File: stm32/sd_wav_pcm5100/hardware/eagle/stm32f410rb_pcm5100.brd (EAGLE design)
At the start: 46 x 58.2 mm, 33 parts, among them IC1 STM32F410_8_B_LQFP64, U5 PCM5100

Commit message: added dirtypcb gerbers
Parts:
- C28, C29: value 2200pF -> 2.2nF
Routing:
- net N$11: track 0.00 -> 208.3 mm
- net VCC: track 257.2 -> 261.4 mm
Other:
- board size 46 x 58.2 mm -> 46.1 x 58.2 mm

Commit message: refactored pcb
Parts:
- JP2: value M023.5MM -> Vsupply - 3.3Vcc
- MMC1: value MICROSD_AMPHENOL -> Amphenol
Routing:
- net N$11: track 208.3 -> 0.00 mm
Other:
- board text added: "+3V3"
- board text added: "3V3"
- board text added: "GND"
- board text added: "NRST"
- board text added: "OUTL"
- board text added: "OUTR"
- board text added: "STANDBY"
- board text added: "SWO"
- board text added: "TCK"
- board text added: "TMS"
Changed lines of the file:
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@@
 <wire x1="46.1772" y1="0" x2="0.127" y2="0" width="0.4064" layer="20"/>
 <wire x1="0.127" y1="0" x2="0.127" y2="58.1152" width="0.4064" layer="20"/>
+<text x="1.8288" y="15.0622" size="0.6096" layer="21" ratio="14" rot="MR270">TMS</text>
+<text x="1.8288" y="17.8562" size="0.6096" layer="21" ratio="14" rot="MR270">GND</text>
+<text x="1.778" y="20.193" size="0.6096" layer="21" ratio="14" rot="MR270">3V3</text>
+<text x="1.7272" y="22.5552" size="0.6096" layer="21" ratio="14" rot="MR270">TCK</text>
+<text x="1.651" y="25.3238" size="0.6096" layer="21" ratio="14" rot="MR270">SWO</text>
+<text x="1.651" y="28.2702" size="0.6096" layer="21" ratio="14" rot="MR270">NRST</text>
+<text x="44.196" y="4.4958" size="0.6096" layer="21" ratio="14" rot="MR270">GND</text>
+<text x="44.0944" y="8.7122" size="0.6096" layer="21" ratio="14" rot="MR270">+3V3</text>
+<text x="30.8356" y="57.2008" size="0.6096" layer="21" ratio="14" rot="MR180">GND</text>
+<text x="34.1884" y="57.2516" size="0.6096" layer="21" ratio="14" rot="MR180">OUTR</text>
+<text x="27.3812" y="57.2516" size="0.6096" layer="21" ratio="14" rot="MR180">OUTL</text>
+<text x="22.5552" y="57.2262" size="0.6096" layer="21" ratio="14" rot="MR180">STANDBY</text>
 </plain>
 <attributes>
@@
 </element>
 <element name="JP1" library="pinhead" package="1X06" value="SWD" x="4.1275" y="20.6375" smashed="yes" rot="R270">
-<attribute name="NAME" x="1.3843" y="20.2311" size="0.6096" layer="25" ratio="10" rot="R270"/>
-<attribute name="VALUE" x="1.3081" y="24.2443" size="0.6096" layer="27" rot="R270"/>
+<attribute name="NAME" x="3.2385" y="12.4587" size="0.6096" layer="26" ratio="10" rot="MR270"/>
+<attribute name="VALUE" x="4.7371" y="12.5349" size="0.6096" layer="28" rot="MR270"/>
 </element>
 <element name="R2" library="SparkFun-Passives" package="0805" value="10K" x="7.239" y="37.2745" smashed="yes" rot="MR180">
@@
 <attribute name="VALUE" x="21.082" y="42.1005" size="0.6096" layer="28" rot="MR0"/>
 </element>
-<element name="MMC1" library="microsd_amphenol" package="MICROSD_AMPHENOL" value="MICROSD_AMPHENOL" x="34.163" y="18.0975" smashed="yes" rot="MR270"/>
+<element name="MMC1" library="microsd_amphenol" package="MICROSD_AMPHENOL" value="Amphenol" x="34.163" y="18.0975" smashed="yes" rot="MR270"/>
 <element name="R3" library="SparkFun-Passives" package="0805" value="22" x="6.8326" y="15.1384" smashed="yes" rot="MR0">
 <attribute name="NAME" x="9.6012" y="15.4305" size="0.6096" layer="26" rot="MR0"/>
@@
 </element>
 <element name="JP7" library="SparkFun-Connectors" package="SCREWTERMINAL-3.5MM-4" value="BTN_8-11" x="4.826" y="6.35" smashed="yes">
-<attribute name="NAME" x="3.556" y="8.89" size="0.6096" layer="25"/>
-<attribute name="VALUE" x="3.556" y="7.62" size="0.6096" layer="27"/>
+<attribute name="NAME" x="9.8806" y="10.9982" size="0.6096" layer="26" rot="MR180"/>
+<attribute name="VALUE" x="11.6332" y="1.4732" size="0.6096" layer="28" rot="MR0"/>
 </element>
 <element name="JP3" library="SparkFun-Connectors" package="SCREWTERMINAL-3.5MM-4" value="BTN_1-4" x="17.018" y="52.578" smashed="yes" rot="R180">
-<attribute name="NAME" x="18.288" y="50.038" size="0.6096" layer="25" rot="R180"/>
-<attribute name="VALUE" x="18.288" y="51.308" size="0.6096" layer="27" rot="R180"/>
+<attribute name="NAME" x="2.8702" y="52.6034" size="0.6096" layer="26" rot="MR90"/>
+<attribute name="VALUE" x="12.9286" y="47.8536" size="0.6096" layer="28" rot="MR0"/>
 </element>
 <element name="JP5" library="SparkFun-Connectors" package="SCREWTERMINAL-3.5MM-3" value="BTN_5-7" x="21.59" y="6.096" smashed="yes">
-<attribute name="NAME" x="20.32" y="8.636" size="0.6096" layer="25"/>
-<attribute name="VALUE" x="20.32" y="7.366" size="0.6096" layer="27"/>
+<attribute name="NAME" x="24.2062" y="10.6426" size="0.6096" layer="26" rot="MR180"/>
+<attribute name="VALUE" x="26.7462" y="1.3208" size="0.6096" layer="28" rot="MR0"/>
 </element>
 <element name="JP6" library="SparkFun-Connectors" package="SCREWTERMINAL-3.5MM-4" value="AUDIO_OUT" x="35.306" y="52.578" smashed="yes" rot="R180">
-<attribute name="NAME" x="36.576" y="50.038" size="0.6096" layer="25" rot="R180"/>
-<attribute name="VALUE" x="36.576" y="51.308" size="0.6096" layer="27" rot="R180"/>
+<attribute name="NAME" x="21.336" y="52.5272" size="0.6096" layer="26" rot="MR90"/>
+<attribute name="VALUE" x="31.1404" y="48.0314" size="0.6096" layer="28" rot="MR0"/>
 </element>
 <element name="IC1" library="pel_stm32" package="LQFP64" value="STM32F410_8_B_LQFP64" x="16.764" y="32.004" smashed="yes" rot="MR270">
@@
 <attribute name="VALUE" x="11.9782" y="33.3289" size="0.508" layer="28" font="vector" ratio="16" rot="MR180"/>
 </element>
-<element name="JP2" library="SparkFun-Connectors" package="SCREWTERMINAL-3.5MM-2" value="M023.5MM" x="39.37" y="4.064" smashed="yes" rot="R90">
+<element name="JP2" library="SparkFun-Connectors" package="SCREWTERMINAL-3.5MM-2" value="Vsupply - 3.3Vcc" x="39.37" y="4.064" smashed="yes" rot="R90">
 <attribute name="PROD_ID" value="CONN-08399" x="39.37" y="4.064" size="1.778" layer="27" rot="R90" display="off"/>
-<attribute name="NAME" x="36.83" y="2.794" size="0.6096" layer="25" rot="R90"/>
-<attribute name="VALUE" x="38.1" y="2.794" size="0.6096" layer="27" rot="R90"/>
+<attribute name="NAME" x="39.9034" y="9.8298" size="0.6096" layer="26" rot="MR0"/>
+<attribute name="VALUE" x="35.2806" y="8.9662" size="0.6096" layer="28" rot="MR270"/>
 </element>
 </elements>
@@
 <wire x1="26.1061" y1="29.254" x2="27.2432" y2="30.3911" width="0.3048" layer="16"/>
 </signal>
-<signal name="N$11">
-<wire x1="0.1778" y1="58.166" x2="46.2026" y2="58.166" width="0.4064" layer="16"/>
-<wire x1="46.2026" y1="58.166" x2="46.2026" y2="0.0762" width="0.4064" layer="16"/>
-<wire x1="46.2026" y1="0.0762" x2="0.127" y2="0.0762" width="0.4064" layer="16"/>
-<wire x1="0.127" y1="0.0762" x2="0.127" y2="58.1406" width="0.4064" layer="16"/>
-</signal>
 </signals>

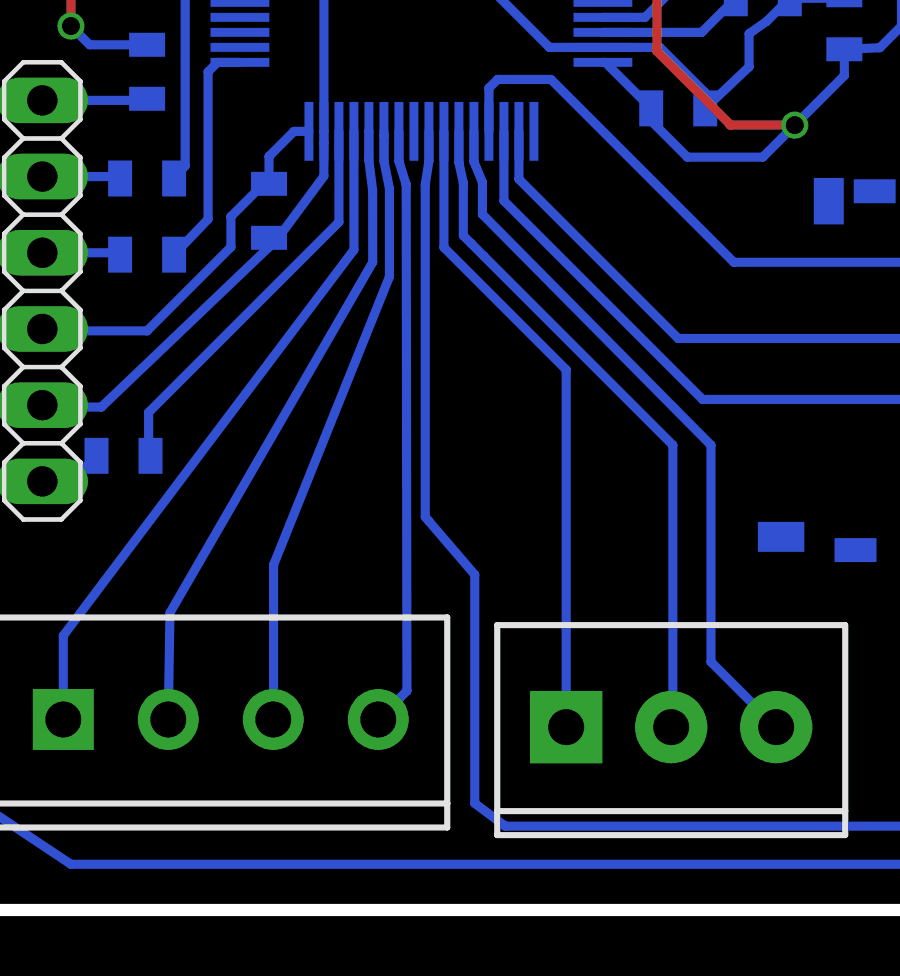
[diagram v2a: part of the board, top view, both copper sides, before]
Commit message: added eagle project libs in one file
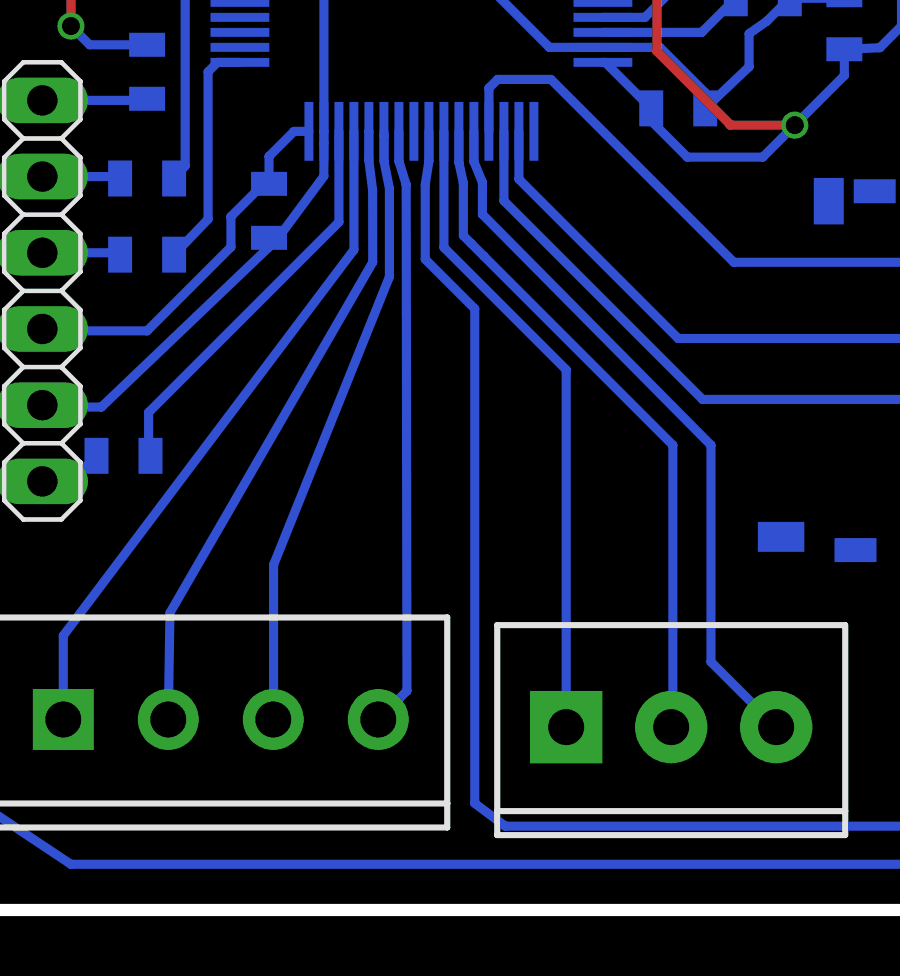
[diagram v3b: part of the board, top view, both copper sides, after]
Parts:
- U5: value PCM5100 -> ROBERTSONICS_PCM5100; device robertsonics:PW_R-PDSO-G20 -> stm32f410rb_pcm5100:ROBERTSONICS_PW_R-PDSO-G20
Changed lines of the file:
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@@
 <attribute name="VALUE" x="36.4617" y="43.7261" size="0.6096" layer="28" font="vector" rot="MR0"/>
 </element>
-<element name="U5" library="robertsonics" package="PW_R-PDSO-G20" value="PCM5100" x="35.687" y="34.036" smashed="yes" rot="MR180">
+<element name="U5" library="stm32f410rb_pcm5100" package="ROBERTSONICS_PW_R-PDSO-G20" value="ROBERTSONICS_PCM5100" x="35.687" y="34.036" smashed="yes" rot="MR180">
 <attribute name="NAME" x="37.2745" y="33.0835" size="0.6096" layer="26" rot="MR180"/>
 <attribute name="VALUE" x="34.0995" y="34.671" size="0.6096" layer="28" rot="MR180"/>
@@
 <wire x1="37.084" y1="14.971059375" x2="38.114940625" y2="16.002" width="0.3048" layer="16"/>
 <wire x1="19.558" y1="2.794" x2="18.542" y2="3.556" width="0.3048" layer="16"/>
-<wire x1="18.542" y1="3.556" x2="18.542" y2="11.176" width="0.3048" layer="16"/>
-<wire x1="18.542" y1="11.176" x2="17.014" y2="12.958" width="0.3048" layer="16"/>
 <wire x1="17.014" y1="25.954" x2="17.014" y2="24.9642" width="0.3048" layer="16"/>
-<wire x1="16.891" y1="13.1064" x2="17.014" y2="12.958" width="0.3048" layer="16"/>
-<wire x1="16.891" y1="24.1808" x2="16.891" y2="13.1064" width="0.3048" layer="16"/>
+<wire x1="16.891" y1="24.1808" x2="16.891" y2="21.6916" width="0.3048" layer="16"/>
 <wire x1="17.014" y1="24.9642" x2="16.891" y2="24.1808" width="0.3048" layer="16"/>
+<wire x1="18.542" y1="3.556" x2="18.542" y2="20.0406" width="0.3048" layer="16"/>
+<wire x1="18.542" y1="20.0406" x2="16.891" y2="21.6916" width="0.3048" layer="16"/>
 </signal>
 <signal name="N$10">
